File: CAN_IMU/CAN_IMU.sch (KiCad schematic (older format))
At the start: 9 parts

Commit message: first commit
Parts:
- added PS?: SBTN01N-05, SamacSys_Parts:SBTN01N05, symbol SamacSys_Parts:SBTN01N-05
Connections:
- net GND: now also PS?.4 (-VOUT)
- new net +24V: PS?.2 (+VIN)
- new net +5V: PS?.5 (+VOUT)
- new net GNDPWR: PS?.1 (-VIN)
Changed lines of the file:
@@
 EESchema Schematic File Version 4
+LIBS:CAN_IMU-cache
 EELAYER 29 0
 EELAYER END
@@
 	1    0    0    -1
 $EndComp
+$Comp
+L SamacSys_Parts:SBTN01N-05 PS?
+U 1 1 5DE65B7E
+P 1250 900
+F 0 "PS?" H 1850 1165 50  0000 C CNN
+F 1 "SBTN01N-05" H 1850 1074 50  0000 C CNN
+F 2 "SamacSys_Parts:SBTN01N05" H 2300 1000 50  0001 L CNN
+F 3 "https://www.meanwell.com/Upload/PDF/SBTN01/SBTN01-SPEC.PDF" H 2300 900 50  0001 L CNN
+F 4 "SBTN01N-05" H 2300 800 50  0001 L CNN "Description"
+F 5 "6.9" H 2300 700 50  0001 L CNN "Height"
+F 6 "Mean Well" H 2300 600 50  0001 L CNN "Manufacturer_Name"
+F 7 "SBTN01N-05" H 2300 500 50  0001 L CNN "Manufacturer_Part_Number"
+F 8 "709-SBTN01N-05" H 2300 400 50  0001 L CNN "Mouser Part Number"
+F 9 "https://www.mouser.com/Search/Refine.aspx?Keyword=709-SBTN01N-05" H 2300 300 50  0001 L CNN "Mouser Price/Stock"
+F 10 "" H 2300 200 50  0001 L CNN "RS Part Number"
+F 11 "" H 2300 100 50  0001 L CNN "RS Price/Stock"
+F 12 "71028311" H 2300 0   50  0001 L CNN "Allied_Number"
+F 13 "https://www.alliedelec.com/meanwellusa-sbtn01n-05/71028311/" H 2300 -100 50  0001 L CNN "Allied Price/Stock"
+	1    1250 900
+	1    0    0    -1
+$EndComp
+$Comp
+L power:+24V #PWR?
+U 1 1 5DE67427
+P 800 1000
+F 0 "#PWR?" H 800 850 50  0001 C CNN
+F 1 "+24V" H 815 1173 50  0000 C CNN
+F 2 "" H 800 1000 50  0001 C CNN
+F 3 "" H 800 1000 50  0001 C CNN
+	1    800  1000
+	1    0    0    -1
+$EndComp
+$Comp
+L power:GNDPWR #PWR?
+U 1 1 5DE67D1C
+P 1250 900
+F 0 "#PWR?" H 1250 700 50  0001 C CNN
+F 1 "GNDPWR" H 1050 850 50  0000 C CNN
+F 2 "" H 1250 850 50  0001 C CNN
+F 3 "" H 1250 850 50  0001 C CNN
+	1    1250 900
+	1    0    0    -1
+$EndComp
+Wire Wire Line
+	800  1000 1250 1000
+$Comp
+L power:+5V #PWR?
+U 1 1 5DE68AE3
+P 2450 900
+F 0 "#PWR?" H 2450 750 50  0001 C CNN
+F 1 "+5V" H 2465 1073 50  0000 C CNN
+F 2 "" H 2450 900 50  0001 C CNN
+F 3 "" H 2450 900 50  0001 C CNN
+	1    2450 900
+	1    0    0    -1
+$EndComp
+$Comp
+L power:GND #PWR?
+U 1 1 5DE692B6
+P 1250 1100
+F 0 "#PWR?" H 1250 850 50  0001 C CNN
+F 1 "GND" H 1255 927 50  0000 C CNN
+F 2 "" H 1250 1100 50  0001 C CNN
+F 3 "" H 1250 1100 50  0001 C CNN
+	1    1250 1100
+	1    0    0    -1
+$EndComp

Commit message: 3.3v reguretor
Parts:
- added C?: 0.1u, Capacitor_SMD:C_0603_1608Metric_Pad1.05x0.95mm_HandSolder, symbol Device:C
- added U?: NJM12888F33, Package_TO_SOT_SMD:SOT-23-5, symbol Regulator_Linear:TLV70212_SOT23-5
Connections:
- net +5V: now also C?.1, U?.1 (IN), U?.3 (EN)
- net GND: now also C?.2, U?.2 (GND)
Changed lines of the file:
@@
 	1    0    0    -1
 $EndComp
+$Comp
+L Regulator_Linear:TLV70212_SOT23-5 U?
+U 1 1 5DE7821C
+P 3900 1050
+F 0 "U?" H 3900 1392 50  0000 C CNN
+F 1 "NJM12888F33" H 3900 1301 50  0000 C CNN
+F 2 "Package_TO_SOT_SMD:SOT-23-5" H 3900 1375 50  0001 C CIN
+F 3 "http://www.ti.com/lit/ds/symlink/tlv702.pdf" H 3900 1100 50  0001 C CNN
+	1    3900 1050
+	1    0    0    -1
+$EndComp
+$Comp
+L Device:C C?
+U 1 1 5DE78FD8
+P 3350 1200
+F 0 "C?" H 3465 1246 50  0000 L CNN
+F 1 "0.1u" H 3465 1155 50  0000 L CNN
+F 2 "Capacitor_SMD:C_0603_1608Metric_Pad1.05x0.95mm_HandSolder" H 3388 1050 50  0001 C CNN
+F 3 "~" H 3350 1200 50  0001 C CNN
+	1    3350 1200
+	1    0    0    -1
+$EndComp
+Wire Wire Line
+	3600 1050 3600 950
+$Comp
+L power:+5V #PWR?
+U 1 1 5DE7AC64
+P 3350 950
+F 0 "#PWR?" H 3350 800 50  0001 C CNN
+F 1 "+5V" H 3365 1123 50  0000 C CNN
+F 2 "" H 3350 950 50  0001 C CNN
+F 3 "" H 3350 950 50  0001 C CNN
+	1    3350 950
+	1    0    0    -1
+$EndComp
+$Comp
+L power:GND #PWR?
+U 1 1 5DE7B2E4
+P 3350 1350
+F 0 "#PWR?" H 3350 1100 50  0001 C CNN
+F 1 "GND" H 3355 1177 50  0000 C CNN
+F 2 "" H 3350 1350 50  0001 C CNN
+F 3 "" H 3350 1350 50  0001 C CNN
+	1    3350 1350
+	1    0    0    -1
+$EndComp
+$Comp
+L power:GND #PWR?
+U 1 1 5DE7B63B
+P 3900 1350
+F 0 "#PWR?" H 3900 1100 50  0001 C CNN
+F 1 "GND" H 3905 1177 50  0000 C CNN
+F 2 "" H 3900 1350 50  0001 C CNN
+F 3 "" H 3900 1350 50  0001 C CNN
+	1    3900 1350
+	1    0    0    -1
+$EndComp
+Wire Wire Line
+	3600 950  3350 950
+Wire Wire Line
+	3350 950  3350 1050
+Connection ~ 3600 950
+Connection ~ 3350 950
 $EndSCHEMATC

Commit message: move
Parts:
- added C?: 0.47u, Capacitor_SMD:C_0603_1608Metric_Pad1.05x0.95mm_HandSolder, symbol Device:C
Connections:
- net +3V3: now also U?.5 (OUT), C?.1
- net GND: now also C?.2
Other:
- moved on the sheet: C?, U?
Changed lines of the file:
@@
 L Regulator_Linear:TLV70212_SOT23-5 U?
 U 1 1 5DE7821C
-P 3900 1050
-F 0 "U?" H 3900 1392 50  0000 C CNN
-F 1 "NJM12888F33" H 3900 1301 50  0000 C CNN
-F 2 "Package_TO_SOT_SMD:SOT-23-5" H 3900 1375 50  0001 C CIN
-F 3 "http://www.ti.com/lit/ds/symlink/tlv702.pdf" H 3900 1100 50  0001 C CNN
-	1    3900 1050
+P 3250 1000
+F 0 "U?" H 3250 1342 50  0000 C CNN
+F 1 "NJM12888F33" H 3250 1251 50  0000 C CNN
+F 2 "Package_TO_SOT_SMD:SOT-23-5" H 3250 1325 50  0001 C CIN
+F 3 "http://www.ti.com/lit/ds/symlink/tlv702.pdf" H 3250 1050 50  0001 C CNN
+	1    3250 1000
 	1    0    0    -1
 $EndComp
@@
 L Device:C C?
 U 1 1 5DE78FD8
-P 3350 1200
-F 0 "C?" H 3465 1246 50  0000 L CNN
-F 1 "0.1u" H 3465 1155 50  0000 L CNN
-F 2 "Capacitor_SMD:C_0603_1608Metric_Pad1.05x0.95mm_HandSolder" H 3388 1050 50  0001 C CNN
-F 3 "~" H 3350 1200 50  0001 C CNN
-	1    3350 1200
+P 2700 1150
+F 0 "C?" H 2815 1196 50  0000 L CNN
+F 1 "0.1u" H 2815 1105 50  0000 L CNN
+F 2 "Capacitor_SMD:C_0603_1608Metric_Pad1.05x0.95mm_HandSolder" H 2738 1000 50  0001 C CNN
+F 3 "~" H 2700 1150 50  0001 C CNN
+	1    2700 1150
 	1    0    0    -1
 $EndComp
 Wire Wire Line
-	3600 1050 3600 950
+	2950 1000 2950 900
 $Comp
 L power:+5V #PWR?
 U 1 1 5DE7AC64
-P 3350 950
-F 0 "#PWR?" H 3350 800 50  0001 C CNN
-F 1 "+5V" H 3365 1123 50  0000 C CNN
-F 2 "" H 3350 950 50  0001 C CNN
-F 3 "" H 3350 950 50  0001 C CNN
-	1    3350 950
+P 2700 900
+F 0 "#PWR?" H 2700 750 50  0001 C CNN
+F 1 "+5V" H 2715 1073 50  0000 C CNN
+F 2 "" H 2700 900 50  0001 C CNN
+F 3 "" H 2700 900 50  0001 C CNN
+	1    2700 900
 	1    0    0    -1
 $EndComp
@@
 L power:GND #PWR?
 U 1 1 5DE7B2E4
-P 3350 1350
-F 0 "#PWR?" H 3350 1100 50  0001 C CNN
-F 1 "GND" H 3355 1177 50  0000 C CNN
-F 2 "" H 3350 1350 50  0001 C CNN
-F 3 "" H 3350 1350 50  0001 C CNN
-	1    3350 1350
+P 2700 1300
+F 0 "#PWR?" H 2700 1050 50  0001 C CNN
+F 1 "GND" H 2705 1127 50  0000 C CNN
+F 2 "" H 2700 1300 50  0001 C CNN
+F 3 "" H 2700 1300 50  0001 C CNN
+	1    2700 1300
 	1    0    0    -1
 $EndComp
@@
 L power:GND #PWR?
 U 1 1 5DE7B63B
-P 3900 1350
-F 0 "#PWR?" H 3900 1100 50  0001 C CNN
-F 1 "GND" H 3905 1177 50  0000 C CNN
-F 2 "" H 3900 1350 50  0001 C CNN
-F 3 "" H 3900 1350 50  0001 C CNN
-	1    3900 1350
+P 3250 1300
+F 0 "#PWR?" H 3250 1050 50  0001 C CNN
+F 1 "GND" H 3255 1127 50  0000 C CNN
+F 2 "" H 3250 1300 50  0001 C CNN
+F 3 "" H 3250 1300 50  0001 C CNN
+	1    3250 1300
 	1    0    0    -1
 $EndComp
 Wire Wire Line
-	3600 950  3350 950
+	2950 900  2700 900
 Wire Wire Line
-	3350 950  3350 1050
-Connection ~ 3600 950
-Connection ~ 3350 950
+	2700 900  2700 1000
+Connection ~ 2950 900
+Connection ~ 2700 900
+$Comp
+L power:+3V3 #PWR?
+U 1 1 5DE7C8AB
+P 3650 900
+F 0 "#PWR?" H 3650 750 50  0001 C CNN
+F 1 "+3V3" H 3665 1073 50  0000 C CNN
+F 2 "" H 3650 900 50  0001 C CNN
+F 3 "" H 3650 900 50  0001 C CNN
+	1    3650 900
+	1    0    0    -1
+$EndComp
+$Comp
+L Device:C C?
+U 1 1 5DE7D144
+P 3650 1150
+F 0 "C?" H 3765 1196 50  0000 L CNN
+F 1 "0.47u" H 3765 1105 50  0000 L CNN
+F 2 "Capacitor_SMD:C_0603_1608Metric_Pad1.05x0.95mm_HandSolder" H 3688 1000 50  0001 C CNN
+F 3 "~" H 3650 1150 50  0001 C CNN
+	1    3650 1150
+	1    0    0    -1
+$EndComp
+Wire Wire Line
+	3650 1000 3650 900
+Wire Wire Line
+	3650 900  3550 900
+Connection ~ 3650 900
+$Comp
+L power:GND #PWR?
+U 1 1 5DE7E724
+P 3650 1300
+F 0 "#PWR?" H 3650 1050 50  0001 C CNN
+F 1 "GND" H 3655 1127 50  0000 C CNN
+F 2 "" H 3650 1300 50  0001 C CNN
+F 3 "" H 3650 1300 50  0001 C CNN
+	1    3650 1300
+	1    0    0    -1
+$EndComp
 $EndSCHEMATC

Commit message: micon
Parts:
- added U?: STM32F042K6Tx, Package_QFP:LQFP-32_7x7mm_P0.8mm, symbol MCU_ST_STM32F0:STM32F042K6Tx
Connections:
- net +3V3: now also U?.1 (VDD), U?.17 (VDDIO2), U?.5 (VDDA)
- net CAN_RX: now also U?.21 (PA11)
- net CAN_TX: now also U?.22 (PA12)
- net GND: now also U?.16 (VSS), U?.32 (VSSA)
- new net OSCIN: U?.2 (PF0)
- new net RESET: U?.4 (NRST)
- new net SCL: U?.31 (PB8)
- new net SDA: U?.30 (PB7)
- new net SWCLK: U?.24 (PA14)
- new net SWDIO: U?.23 (PA13)
- no-connect marks 0 -> 1
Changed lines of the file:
@@
 	1    0    0    -1
 $EndComp
+$Comp
+L MCU_ST_STM32F0:STM32F042K6Tx U?
+U 1 1 5DE77FCA
+P 3200 3800
+F 0 "U?" H 3550 2750 50  0000 C CNN
+F 1 "STM32F042K6Tx" H 3550 2850 50  0000 C CNN
+F 2 "Package_QFP:LQFP-32_7x7mm_P0.8mm" H 2800 2900 50  0001 R CNN
+F 3 "http://www.st.com/st-web-ui/static/active/en/resource/technical/document/datasheet/DM00105814.pdf" H 3200 3800 50  0001 C CNN
+	1    3200 3800
+	1    0    0    -1
+$EndComp
+$Comp
+L power:+3V3 #PWR?
+U 1 1 5DE7A1A5
+P 3200 2800
+F 0 "#PWR?" H 3200 2650 50  0001 C CNN
+F 1 "+3V3" H 3215 2973 50  0000 C CNN
+F 2 "" H 3200 2800 50  0001 C CNN
+F 3 "" H 3200 2800 50  0001 C CNN
+	1    3200 2800
+	1    0    0    -1
+$EndComp
+Wire Wire Line
+	3300 2900 3300 2800
+Wire Wire Line
+	3300 2800 3200 2800
+Wire Wire Line
+	3100 2800 3100 2900
+Connection ~ 3200 2800
+Wire Wire Line
+	3200 2800 3100 2800
+Wire Wire Line
+	3200 2900 3200 2800
+$Comp
+L power:GND #PWR?
+U 1 1 5DE7B378
+P 3150 4850
+F 0 "#PWR?" H 3150 4600 50  0001 C CNN
+F 1 "GND" H 3155 4677 50  0000 C CNN
+F 2 "" H 3150 4850 50  0001 C CNN
+F 3 "" H 3150 4850 50  0001 C CNN
+	1    3150 4850
+	1    0    0    -1
+$EndComp
+Wire Wire Line
+	3200 4800 3200 4850
+Wire Wire Line
+	3200 4850 3150 4850
+Wire Wire Line
+	3100 4800 3100 4850
+Wire Wire Line
+	3100 4850 3150 4850
+Connection ~ 3150 4850
+Text Label 2450 3600 0    50   ~ 0
+OSCIN
+Wire Wire Line
+	2450 3600 2700 3600
+NoConn ~ 2700 3700
+Text Label 2450 4600 0    50   ~ 0
+SCL
+Text Label 2450 4500 0    50   ~ 0
+SDA
+Wire Wire Line
+	2450 4500 2700 4500
+Wire Wire Line
+	2700 4600 2450 4600
+Text GLabel 3700 4300 2    50   Output ~ 0
+CAN_TX
+Text GLabel 3700 4200 2    50   Output ~ 0
+CAN_RX
+Text GLabel 3700 4400 2    50   Input ~ 0
+SWDIO
+Text GLabel 3700 4500 2    50   Input ~ 0
+SWCLK
+Text GLabel 2700 3100 0    50   Input ~ 0
+RESET
 $EndSCHEMATC

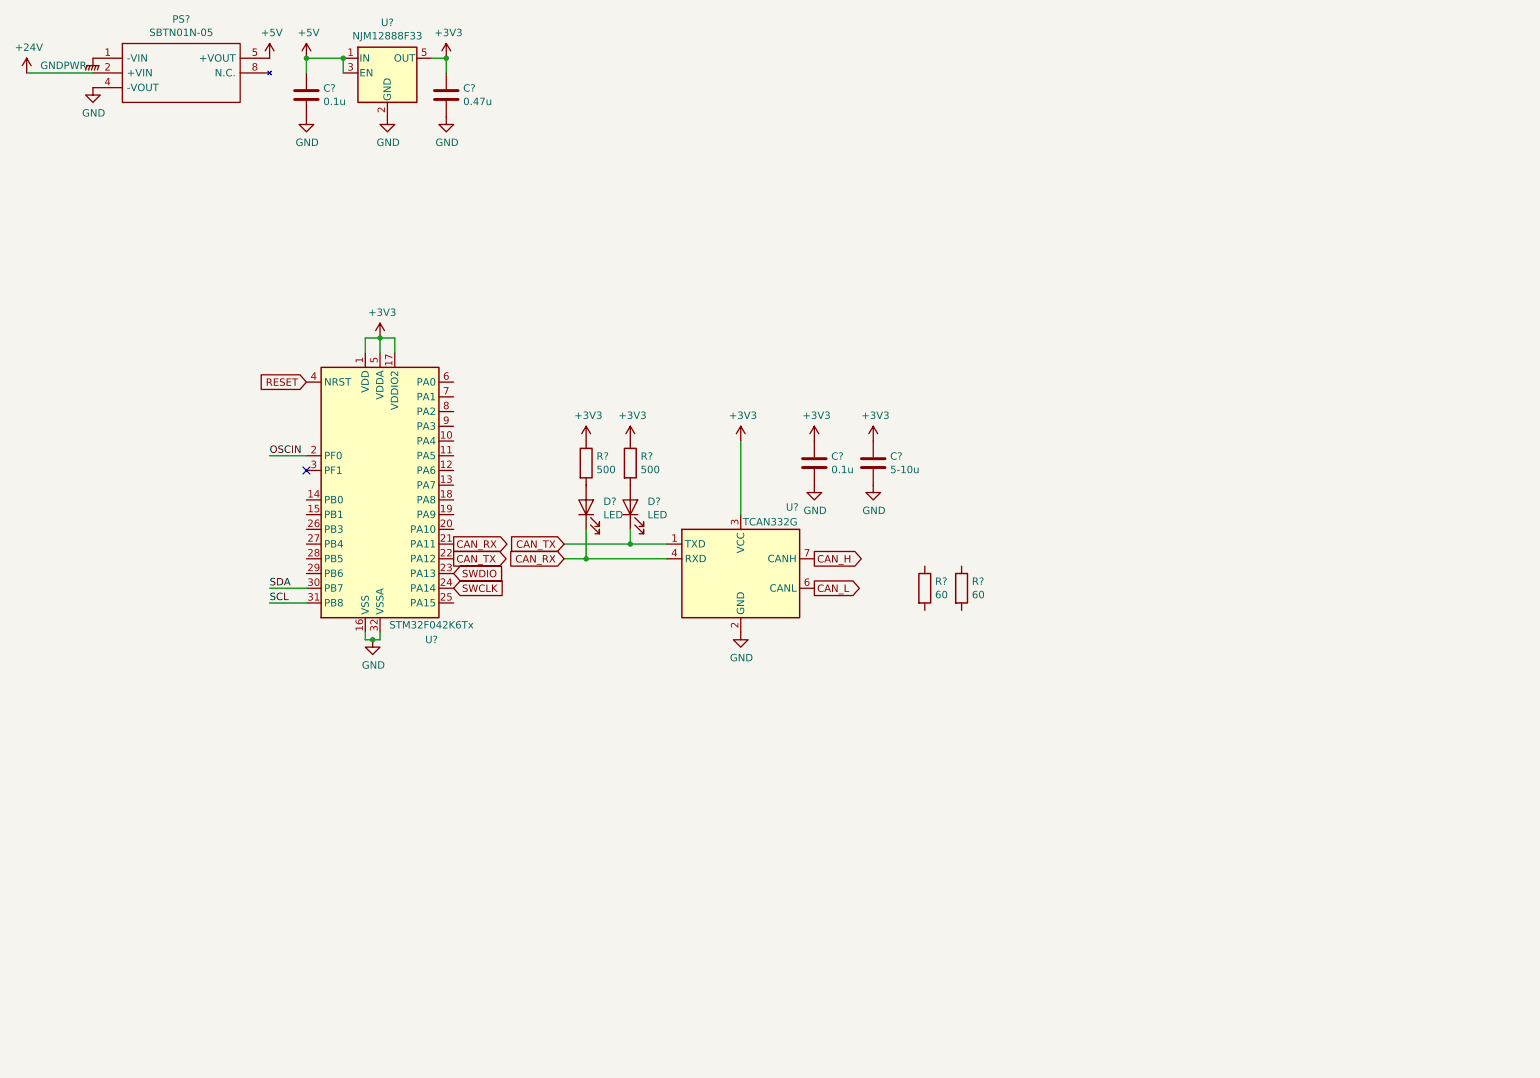
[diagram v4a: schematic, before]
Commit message: STMに変更
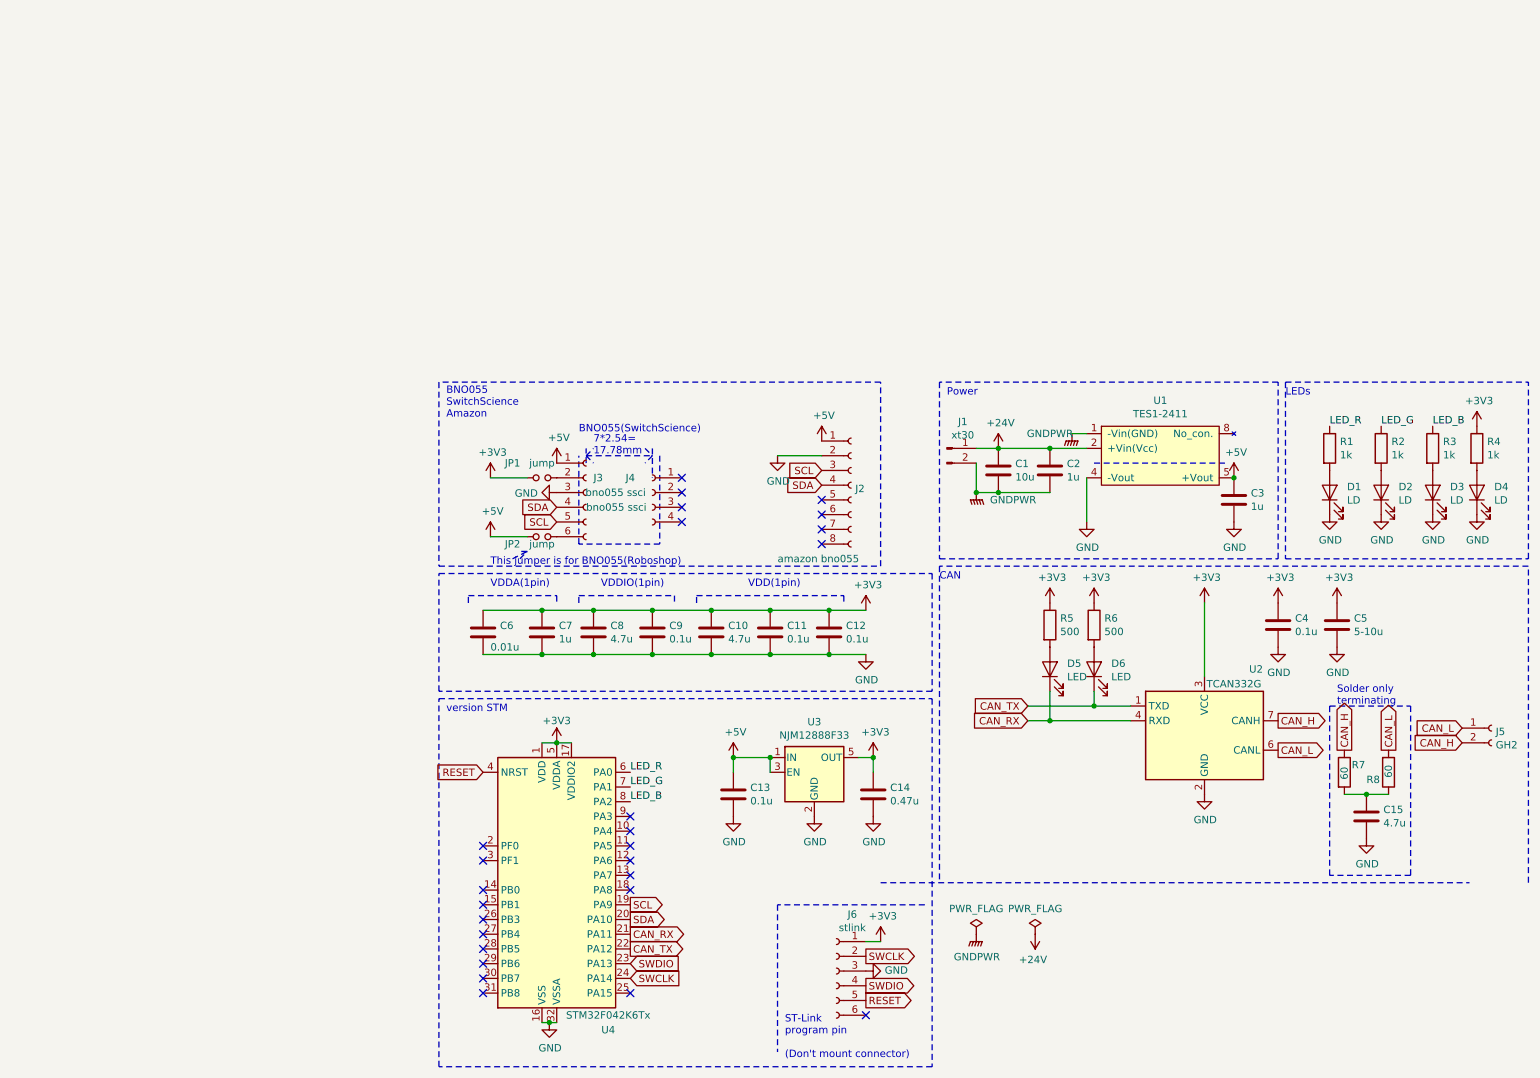
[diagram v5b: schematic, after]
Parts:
- removed PS?: SBTN01N-05, SamacSys_Parts:SBTN01N05, symbol SamacSys_Parts:SBTN01N-05
- added C1: 10u, Capacitor_SMD:C_0603_1608Metric_Pad1.05x0.95mm_HandSolder, symbol Device:C
- added C10, C15, C8: 4.7u, Capacitor_SMD:C_0603_1608Metric_Pad1.05x0.95mm_HandSolder, symbol Device:C
- added C11, C12, C9: 0.1u, Capacitor_SMD:C_0603_1608Metric_Pad1.05x0.95mm_HandSolder, symbol Device:C
- added C2, C3, C7: 1u, Capacitor_SMD:C_0603_1608Metric_Pad1.05x0.95mm_HandSolder, symbol Device:C
- added C6: 0.01u, Capacitor_SMD:C_0603_1608Metric_Pad1.05x0.95mm_HandSolder, symbol Device:C
- added D1, D2, D3, D4: LD, LED_SMD:LED_0603_1608Metric_Pad1.05x0.95mm_HandSolder, symbol Device:LED
- added J1: xt30, Connector_AMASS:AMASS_XT30PW-M_1x02_P2.50mm_Horizontal, symbol Connector:Conn_01x02_Male
- added J2: amazon bno055, Connector_PinSocket_2.54mm:PinSocket_1x08_P2.54mm_Vertical_SMD_Pin1Left, symbol Connector:Conn_01x08_Female
- added J3: bno055 ssci, Connector_PinSocket_2.54mm:PinSocket_1x06_P2.54mm_Vertical_SMD_Pin1Left, symbol Connector:Conn_01x06_Female
- added J4: bno055 ssci, Connector_PinSocket_2.54mm:PinSocket_1x04_P2.54mm_Vertical_SMD_Pin1Left, symbol Connector:Conn_01x04_Female
- added J5: GH2, Connector_JST:JST_GH_SM02B-GHS-TB_1x02-1MP_P1.25mm_Horizontal, symbol Connector:Conn_01x02_Female
- added J6: stlink, Connector_PinHeader_2.54mm:PinHeader_1x06_P2.54mm_Vertical, symbol Connector:Conn_01x06_Female
- added JP1, JP2: jump, Jumper:SolderJumper-2_P1.3mm_Open_RoundedPad1.0x1.5mm, symbol Device:Jumper_NO_Small
- added R1, R2, R3, R4: 1k, Resistor_SMD:R_0603_1608Metric_Pad1.05x0.95mm_HandSolder, symbol Device:R
- added U1: TES1-2411, Morita:TES1-single, symbol Morita:TES2-2411H
- gave numbers to parts that had none: 13
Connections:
- net +24V: now also C1.1, C2.1, J1.1 (Pin_1), U1.2 (+Vin(Vcc))
- net +3V3: now also C10.1, C11.1, C12.1, C6.1, C7.1, C8.1, C9.1, J6.1 (Pin_1), JP1.1, R4.1
- net +5V: now also C3.1, J2.1 (Pin_1), J3.1 (Pin_1), JP2.1, U1.5 (+Vout)
- net CAN_H: now also R7.1, J5.2 (Pin_2)
- net CAN_L: now also R8.2, J5.1 (Pin_1)
- net GND: now also C10.2, C11.2, C12.2, C15.2, C3.2, C6.2, C7.2, C8.2, C9.2, D1.1 (K), D2.1 (K), D3.1 (K), D4.1 (K), J2.2 (Pin_2), J3.3 (Pin_3), J6.3 (Pin_3), U1.4 (-Vout)
- net GNDPWR: now also C1.2, C2.2, J1.2 (Pin_2), U1.1 (-Vin(GND))
- net RESET: now also J6.5 (Pin_5)
- net SCL: now also U4.19 (PA9), J2.3 (Pin_3), J3.5 (Pin_5); no longer U4.31 (PB8)
- net SDA: now also U4.20 (PA10), J2.4 (Pin_4), J3.4 (Pin_4); no longer U4.30 (PB7)
- net SWCLK: now also J6.2 (Pin_2)
- net SWDIO: now also J6.4 (Pin_4)
- net at R8.1: now also R7.2, C15.1
- net LED_R: now reaches U4.6 (PA0)
- net LED_R: now also R1.1
- net LED_G: now reaches U4.7 (PA1)
- net LED_G: now also R2.1
- net LED_B: now reaches U4.8 (PA2)
- net LED_B: now also R3.1
- net OSCIN: no longer names the net of U4.2 (PF0)
- new net: J3.2 (Pin_2), JP1.2
- new net: J3.6 (Pin_6), JP2.2
- new net: D4.2 (A), R4.2
- new net: D3.2 (A), R3.2
- new net: D2.2 (A), R2.2
- new net: D1.2 (A), R1.2
- no-connect marks 1 -> 26
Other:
- note added: "7*2.54=\n17.78mm"
- note added: "BNO055(SwitchScience)"
- note added: "BNO055\nSwitchScience\nAmazon"
- note added: "CAN"
- note added: "LEDs"
- note added: "Power"
- note added: "ST-Link\nprogram pin\n\n(Don't mount connector)"
- note added: "Solder only\nterminating"
- note added: "This jumper is for BNO055(Roboshop)"
- note added: "VDD(1pin)"
- note added: "VDDA(1pin)"
- note added: "VDDIO(1pin)"
- note added: "version STM"
- moved on the sheet: C13, C14, C4, C5, D5, D6, R5, R6, R7, R8, U2, U3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

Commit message: 一応完成
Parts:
- removed JP1: jump, Jumper:SolderJumper-2_P1.3mm_Open_RoundedPad1.0x1.5mm, symbol Device:Jumper_NO_Small
- added C1: 10u, Capacitor_SMD:C_0603_1608Metric_Pad1.05x0.95mm_HandSolder, symbol Device:C
- renumbered C9 to C10, C10 to C11, C11 to C12, C12 to C13, C13 to C14, C14 to C15, C15 to C16, C1 to C2, C2 to C3, C3 to C4, C4 to C5, C5 to C6, C6 to C7, C7 to C8, C8 to C9, JP2 to JP1
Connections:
- net +24V: now also J1.2 (Pin_2); no longer J1.1 (Pin_1)
- net +5V: now also C1.1
- net GND: now also C1.2
- net GNDPWR: now also J1.1 (Pin_1); no longer J1.2 (Pin_2)
- net LED_B: now also U4.12 (PA6); no longer U4.8 (PA2)
- net LED_G: now also U4.13 (PA7); no longer U4.7 (PA1)
- net LED_R: now also U4.14 (PB0); no longer U4.6 (PA0)
- no-connect marks 26 -> 27
